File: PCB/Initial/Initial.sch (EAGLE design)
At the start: 44 parts, among them U2 AT24C512C-SHD-B

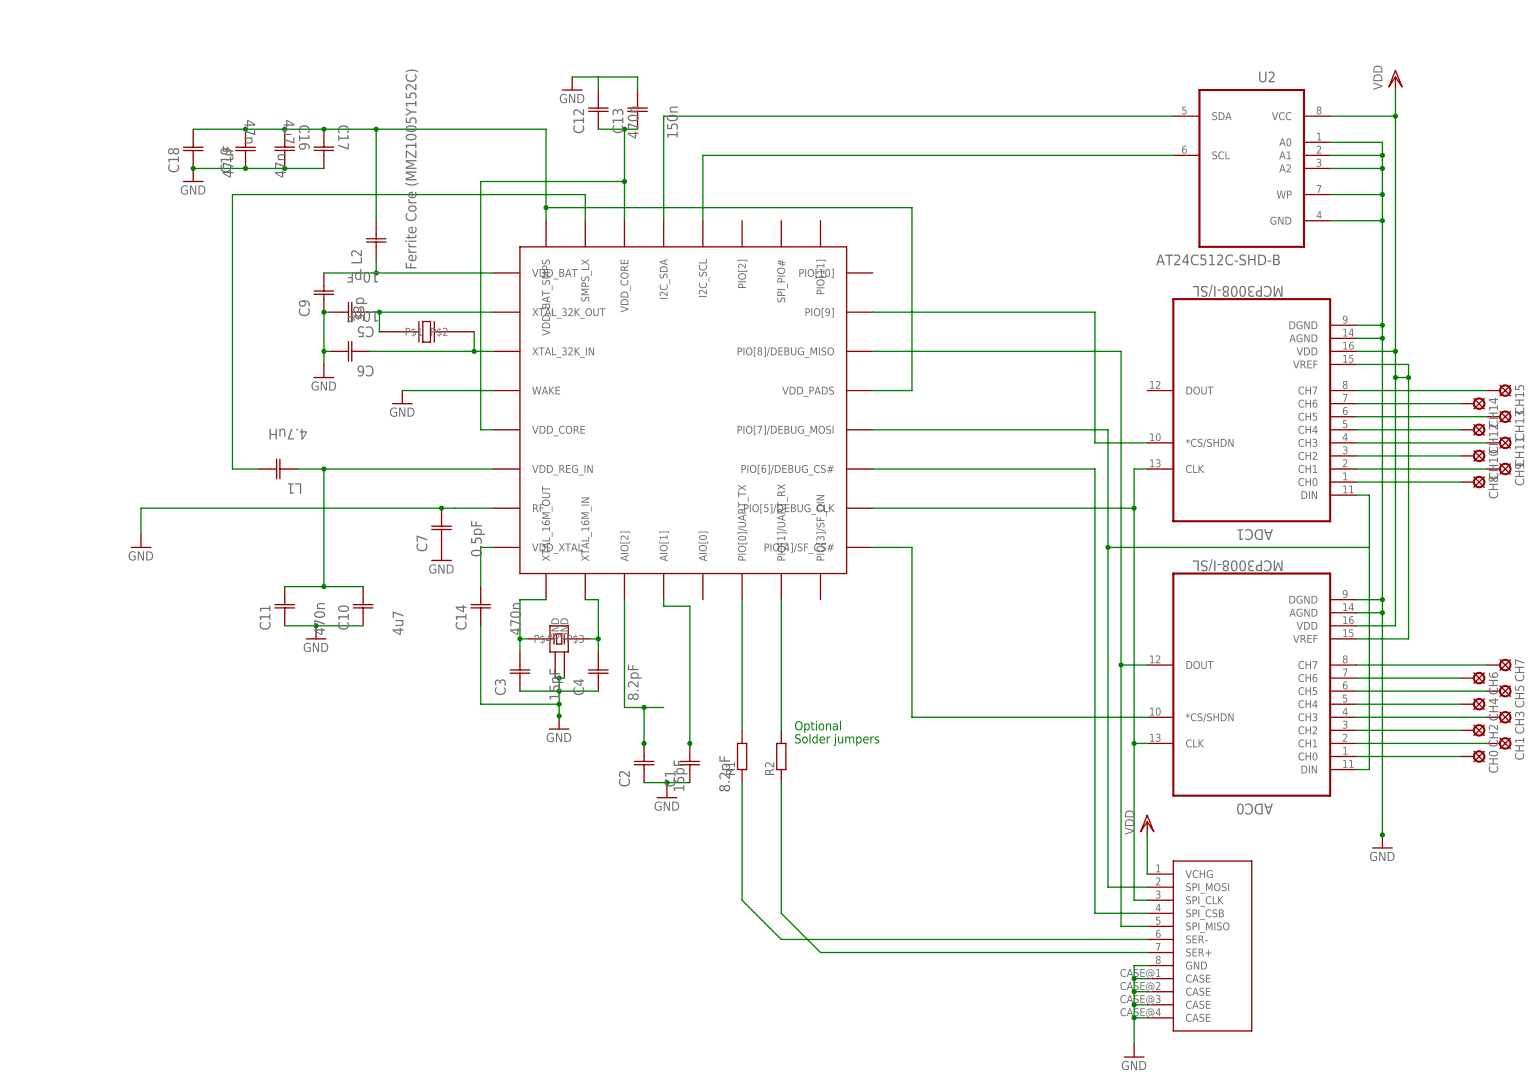
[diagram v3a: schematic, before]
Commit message: Need datasheet for 8 pin connector
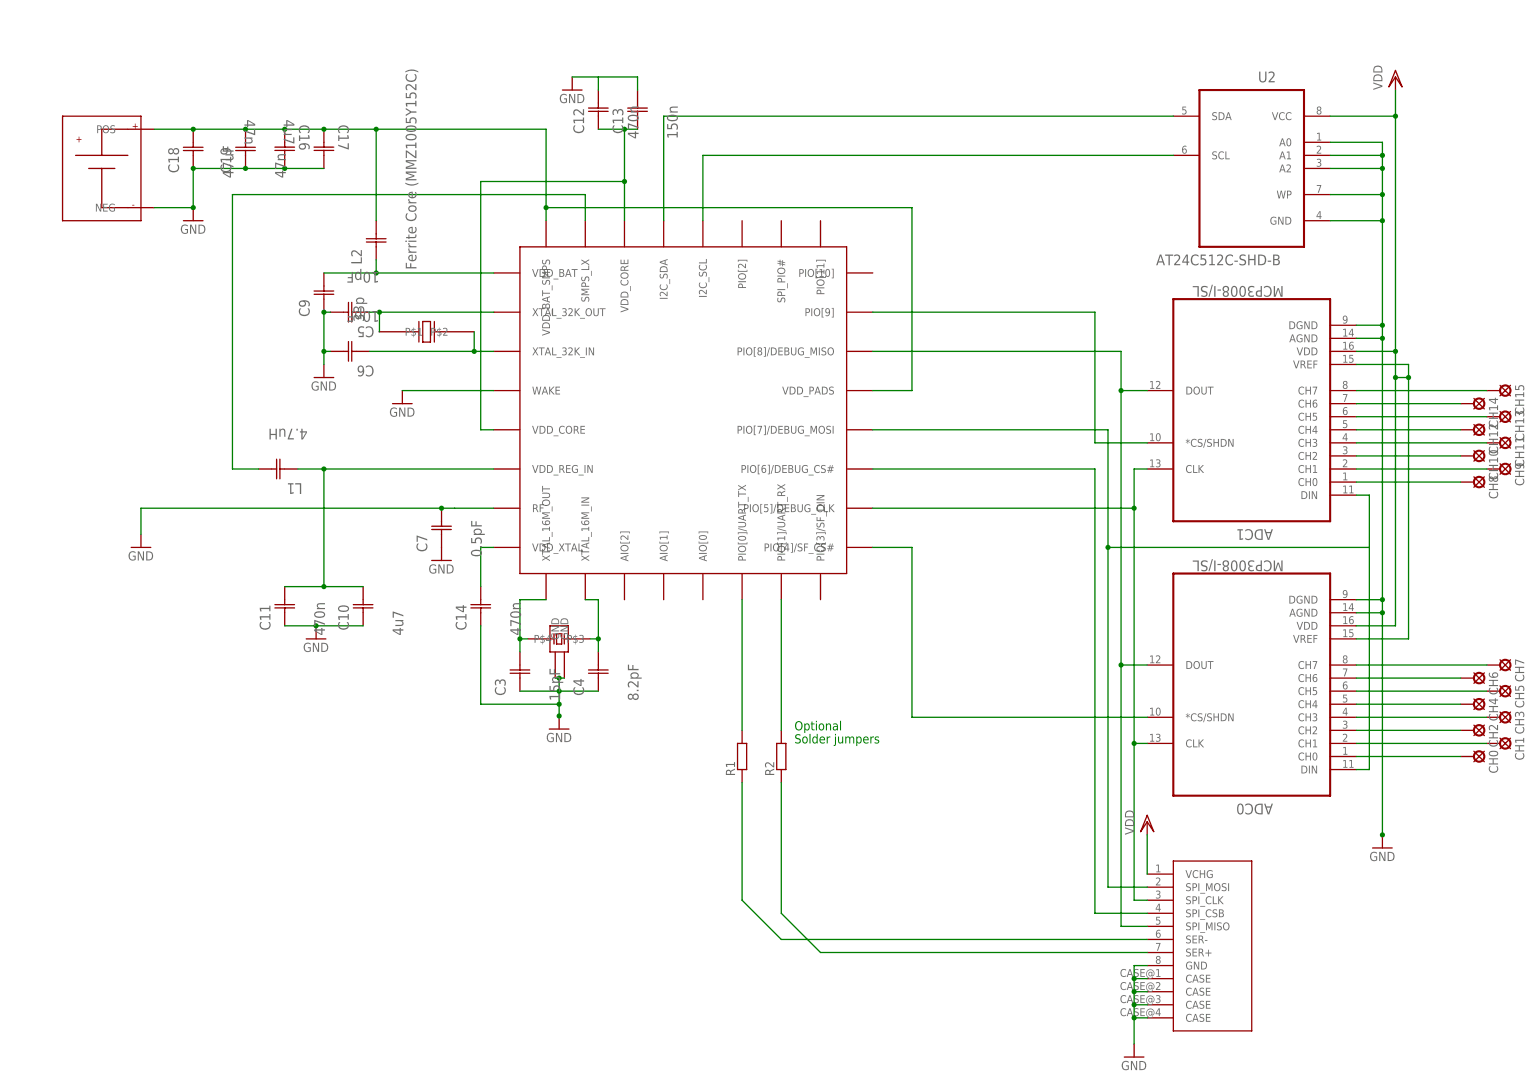
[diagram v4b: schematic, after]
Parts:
- removed C1: 8.2pF, AVX_By_element14_Batch_1:UQCL2A8R2CAT2A/500
- removed C2: 15pF, AVX_By_element14_Batch_1:UQCL2A150JAT2A/500
- added U$5: BATTERY_2996, BATTERY_2996:BATTERY_2996
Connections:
- removed net N$33: C1.C2, U$1.AIO[1]
- removed net N$41: C2.C2, U$1.AIO[2]
- removed net N$42: C1.C1, C2.C1
- net GND: now also U$5.NEG
- net N$22: now also ADC1.DOUT
- net N$34: now also U$5.POS
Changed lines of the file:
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@@
 <part name="U$3" library="TSX3225" deviceset="TSX3225" device=""/>
 <part name="U$4" library="SSP-T7-F" deviceset="SSP-T7-F" device=""/>
-<part name="C1" library="AVX_By_element14_Batch_1" deviceset="UQCL2A8R2CAT2A/500" device="" value="8.2pF"/>
-<part name="C2" library="AVX_By_element14_Batch_1" deviceset="UQCL2A150JAT2A/500" device="" value="15pF"/>
-<part name="GND11" library="supply1" deviceset="GND" device=""/>
+<part name="U$5" library="BATTERY_2996" deviceset="BATTERY_2996" device=""/>
 </parts>
 <sheets>
@@
 <instance part="C16" gate="A" x="-137.16" y="109.22" rot="R270"/>
 <instance part="C17" gate="A" x="-129.54" y="109.22" rot="R270"/>
-<instance part="GND10" gate="1" x="-154.94" y="99.06"/>
+<instance part="GND10" gate="1" x="-154.94" y="91.44"/>
 <instance part="U$2" gate="G$1" x="43.18" y="-48.26"/>
 <instance part="VDD2" gate="G$1" x="30.48" y="-25.4"/>
@@
 <instance part="U$3" gate="G$1" x="-83.82" y="10.16" rot="R90"/>
 <instance part="U$4" gate="G$1" x="-100.33" y="69.85" rot="R270"/>
-<instance part="C1" gate="A" x="-58.42" y="-17.78" rot="R90"/>
-<instance part="C2" gate="A" x="-67.31" y="-17.78" rot="R90"/>
-<instance part="GND11" gate="1" x="-62.865" y="-20.701"/>
+<instance part="U$5" gate="G$1" x="-172.72" y="101.6"/>
 </instances>
 <busses>
@@
 <pinref part="U$2" gate="G$1" pin="SPI_MISO"/>
 <wire x1="25.4" y1="-45.72" x2="30.48" y2="-45.72" width="0.1524" layer="91"/>
-<wire x1="25.4" y1="5.08" x2="25.4" y2="66.04" width="0.1524" layer="91"/>
+<wire x1="25.4" y1="5.08" x2="25.4" y2="58.42" width="0.1524" layer="91"/>
 <junction x="25.4" y="5.08"/>
 <pinref part="U$1" gate="G$1" pin="PIO[8]/DEBUG_MISO"/>
+<wire x1="25.4" y1="58.42" x2="25.4" y2="66.04" width="0.1524" layer="91"/>
 <wire x1="25.4" y1="66.04" x2="-22.86" y2="66.04" width="0.1524" layer="91"/>
+<pinref part="ADC1" gate="A" pin="DOUT"/>
+<wire x1="30.48" y1="58.42" x2="25.4" y2="58.42" width="0.1524" layer="91"/>
+<junction x="25.4" y="58.42"/>
 </segment>
 </net>
@@
 </segment>
 <segment>
+<pinref part="C18" gate="A" pin="C1"/>
 <pinref part="GND10" gate="1" pin="GND"/>
+<wire x1="-154.94" y1="93.98" x2="-154.94" y2="101.6" width="0.1524" layer="91"/>
+<pinref part="U$5" gate="G$1" pin="NEG"/>
+<wire x1="-162.56" y1="93.98" x2="-154.94" y2="93.98" width="0.1524" layer="91"/>
+<junction x="-154.94" y="93.98"/>
 <pinref part="C17" gate="A" pin="C2"/>
 <pinref part="C16" gate="A" pin="C2"/>
@@
 <junction x="-137.16" y="101.6"/>
 <wire x1="-137.16" y1="101.6" x2="-144.78" y2="101.6" width="0.1524" layer="91"/>
-<pinref part="C18" gate="A" pin="C1"/>
+<pinref part="C19" gate="A" pin="C1"/>
+<wire x1="-154.94" y1="101.6" x2="-144.78" y2="101.6" width="0.1524" layer="91"/>
 <junction x="-154.94" y="101.6"/>
-<pinref part="C19" gate="A" pin="C1"/>
-<wire x1="-144.78" y1="101.6" x2="-154.94" y2="101.6" width="0.1524" layer="91"/>
 <junction x="-144.78" y="101.6"/>
 </segment>
@@
 <wire x1="-144.78" y1="109.22" x2="-154.94" y2="109.22" width="0.1524" layer="91"/>
 <junction x="-144.78" y="109.22"/>
+<pinref part="U$5" gate="G$1" pin="POS"/>
+<wire x1="-154.94" y1="109.22" x2="-162.56" y2="109.22" width="0.1524" layer="91"/>
+<junction x="-154.94" y="109.22"/>
 </segment>
 </net>
@@
 </segment>
 </net>
-<net name="N$33" class="0">
-<segment>
-<pinref part="U$1" gate="G$1" pin="AIO[1]"/>
-<wire x1="-63.5" y1="17.78" x2="-63.5" y2="16.51" width="0.1524" layer="91"/>
-<wire x1="-63.5" y1="16.51" x2="-58.42" y2="16.51" width="0.1524" layer="91"/>
-<wire x1="-58.42" y1="16.51" x2="-58.42" y2="-10.16" width="0.1524" layer="91"/>
-<pinref part="C1" gate="A" pin="C2"/>
-<wire x1="-58.42" y1="-10.16" x2="-58.42" y2="-10.795" width="0.1524" layer="91"/>
-<junction x="-58.42" y="-10.16"/>
-</segment>
-</net>
-<net name="N$41" class="0">
-<segment>
-<pinref part="U$1" gate="G$1" pin="AIO[2]"/>
-<wire x1="-63.5" y1="-3.175" x2="-67.31" y2="-3.175" width="0.1524" layer="91"/>
-<wire x1="-67.31" y1="-3.175" x2="-71.12" y2="-3.175" width="0.1524" layer="91"/>
-<wire x1="-71.12" y1="-3.175" x2="-71.12" y2="17.78" width="0.1524" layer="91"/>
-<wire x1="-67.31" y1="-3.175" x2="-67.31" y2="-10.16" width="0.1524" layer="91"/>
-<junction x="-67.31" y="-3.175"/>
-<pinref part="C2" gate="A" pin="C2"/>
-<wire x1="-67.31" y1="-10.16" x2="-67.31" y2="-10.795" width="0.1524" layer="91"/>
-<junction x="-67.31" y="-10.16"/>
-</segment>
-</net>
-<net name="N$42" class="0">
-<segment>
-<pinref part="C2" gate="A" pin="C1"/>
-<pinref part="C1" gate="A" pin="C1"/>
-<wire x1="-67.31" y1="-17.78" x2="-62.865" y2="-17.78" width="0.1524" layer="91"/>
-<wire x1="-62.865" y1="-17.78" x2="-58.42" y2="-17.78" width="0.1524" layer="91"/>
-<wire x1="-62.865" y1="-17.78" x2="-62.865" y2="-18.415" width="0.1524" layer="91"/>
-<junction x="-62.865" y="-17.78"/>
-</segment>
-</net>

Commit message: need to do some bloody exercise. added list of TODOs on schem
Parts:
- added PAD1, PAD2, PAD3, PAD4, PAD5, PAD6: (no value), wirepad:1,6/0,8
- added R3: (no value), resistor-shunt:BVS
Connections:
- new net N$33: PAD1.P, U$1.AIO[2]
- new net N$41: PAD2.P, U$1.AIO[1]
- new net N$42: PAD3.P, U$1.AIO[0]
- new net N$43: PAD4.P, U$1.PIO[3]/SF_DIN
- new net N$44: PAD5.P, U$1.PIO[10]
- new net N$45: R3.1, U$1.SPI_PIO#
- new net N$46: U$1.PIO[2]
- new net N$47: PAD6.P, U$1.PIO[11]
- net VDD: now also R3.2
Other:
- note added: "50 ohms RF"
- note added: "CAP for I2C"
- note added: "Inductor Coils"
- note added: "Push button"
- note added: "add test pads"
- note added: "check SPI will work"
- note added: "mini 8 pin connector"
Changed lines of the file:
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@@
 <part name="U$4" library="SSP-T7-F" deviceset="SSP-T7-F" device=""/>
 <part name="U$5" library="BATTERY_2996" deviceset="BATTERY_2996" device=""/>
+<part name="PAD1" library="wirepad" deviceset="1,6/0,8" device=""/>
+<part name="PAD2" library="wirepad" deviceset="1,6/0,8" device=""/>
+<part name="PAD3" library="wirepad" deviceset="1,6/0,8" device=""/>
+<part name="PAD4" library="wirepad" deviceset="1,6/0,8" device=""/>
+<part name="PAD5" library="wirepad" deviceset="1,6/0,8" device=""/>
+<part name="R3" library="resistor-shunt" deviceset="BVS" device=""/>
+<part name="PAD6" library="wirepad" deviceset="1,6/0,8" device=""/>
 </parts>
 <sheets>
@@
 <text x="-38.1" y="-7.62" size="1.778" layer="91">Optional</text>
 <text x="-38.1" y="-10.16" size="1.778" layer="91">Solder jumpers</text>
+<text x="-190.5" y="62.23" size="1.778" layer="91">50 ohms RF</text>
+<text x="-190.5" y="58.42" size="1.778" layer="91">Inductor Coils</text>
+<text x="-190.5" y="54.61" size="1.778" layer="91">mini 8 pin connector</text>
+<text x="-190.5" y="50.8" size="1.778" layer="91">check SPI will work</text>
+<text x="-190.5" y="46.99" size="1.778" layer="91">add test pads</text>
+<text x="-190.5" y="43.18" size="1.778" layer="91">Push button</text>
+<text x="-190.5" y="39.37" size="1.778" layer="91">CAP for I2C</text>
 </plain>
 <instances>
@@
 <instance part="U$4" gate="G$1" x="-100.33" y="69.85" rot="R270"/>
 <instance part="U$5" gate="G$1" x="-172.72" y="101.6"/>
+<instance part="PAD1" gate="P" x="-71.12" y="15.24" rot="R90"/>
+<instance part="PAD2" gate="P" x="-63.5" y="15.24" rot="R90"/>
+<instance part="PAD3" gate="P" x="-55.88" y="15.24" rot="R90"/>
+<instance part="PAD4" gate="P" x="-33.02" y="15.24" rot="R90"/>
+<instance part="PAD5" gate="P" x="-20.32" y="81.28" rot="MR0"/>
+<instance part="R3" gate="G$1" x="1.27" y="85.09" rot="R180"/>
+<instance part="PAD6" gate="P" x="-33.02" y="95.25" rot="R270"/>
 </instances>
 <busses>
@@
 <pinref part="ADC0" gate="A" pin="VDD"/>
 <wire x1="78.74" y1="60.96" x2="78.74" y2="12.7" width="0.1524" layer="91"/>
-<wire x1="78.74" y1="66.04" x2="78.74" y2="111.76" width="0.1524" layer="91"/>
+<wire x1="78.74" y1="66.04" x2="78.74" y2="85.09" width="0.1524" layer="91"/>
 <pinref part="U2" gate="A" pin="VCC"/>
+<wire x1="78.74" y1="85.09" x2="78.74" y2="111.76" width="0.1524" layer="91"/>
 <wire x1="66.04" y1="111.76" x2="78.74" y2="111.76" width="0.1524" layer="91"/>
 <wire x1="71.12" y1="66.04" x2="78.74" y2="66.04" width="0.1524" layer="91"/>
@@
 <junction x="81.28" y="60.96"/>
 <junction x="78.74" y="60.96"/>
+<pinref part="R3" gate="G$1" pin="2"/>
+<wire x1="6.35" y1="85.09" x2="78.74" y2="85.09" width="0.1524" layer="91"/>
+<junction x="78.74" y="85.09"/>
 </segment>
 <segment>
@@
 </segment>
 </net>
+<net name="N$33" class="0">
+<segment>
+<pinref part="U$1" gate="G$1" pin="AIO[2]"/>
+<pinref part="PAD1" gate="P" pin="P"/>
+</segment>
+</net>
+<net name="N$41" class="0">
+<segment>
+<pinref part="U$1" gate="G$1" pin="AIO[1]"/>
+<pinref part="PAD2" gate="P" pin="P"/>
+</segment>
+</net>
+<net name="N$42" class="0">
+<segment>
+<pinref part="U$1" gate="G$1" pin="AIO[0]"/>
+<pinref part="PAD3" gate="P" pin="P"/>
+</segment>
+</net>
+<net name="N$43" class="0">
+<segment>
+<pinref part="U$1" gate="G$1" pin="PIO[3]/SF_DIN"/>
+<pinref part="PAD4" gate="P" pin="P"/>
+</segment>
+</net>
+<net name="N$44" class="0">
+<segment>
+<pinref part="U$1" gate="G$1" pin="PIO[10]"/>
+<pinref part="PAD5" gate="P" pin="P"/>
+</segment>
+</net>
+<net name="N$45" class="0">
+<segment>
+<pinref part="U$1" gate="G$1" pin="SPI_PIO#"/>
+<wire x1="-40.64" y1="91.44" x2="-40.64" y2="97.79" width="0.1524" layer="91"/>
+<wire x1="-40.64" y1="97.79" x2="-5.08" y2="97.79" width="0.1524" layer="91"/>
+<wire x1="-5.08" y1="97.79" x2="-5.08" y2="85.09" width="0.1524" layer="91"/>
+<pinref part="R3" gate="G$1" pin="1"/>
+<wire x1="-5.08" y1="85.09" x2="-3.81" y2="85.09" width="0.1524" layer="91"/>
+</segment>
+</net>
+<net name="N$46" class="0">
+<segment>
+<pinref part="U$1" gate="G$1" pin="PIO[2]"/>
+<wire x1="-48.26" y1="91.44" x2="-48.26" y2="120.65" width="0.1524" layer="91"/>
+<wire x1="-48.26" y1="120.65" x2="69.85" y2="120.65" width="0.1524" layer="91"/>
+<wire x1="69.85" y1="120.65" x2="69.85" y2="114.3" width="0.1524" layer="91"/>
+</segment>
+</net>
+<net name="N$47" class="0">
+<segment>
+<pinref part="U$1" gate="G$1" pin="PIO[11]"/>
+<pinref part="PAD6" gate="P" pin="P"/>
+<wire x1="-33.02" y1="91.44" x2="-33.02" y2="92.71" width="0.1524" layer="91"/>
+</segment>
+</net>
